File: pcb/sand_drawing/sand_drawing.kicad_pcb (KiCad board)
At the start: 2 copper layers, 75.6 x 36.2 mm, 21 parts, among them J0 12V GND, J1 Stepper1, J2 Stepper2, J3 Opto 1, J4 Opto 2, J5 ESP POWER, J6 Unused Pins, U1 WeMos_D1_mini, U2 LD1117

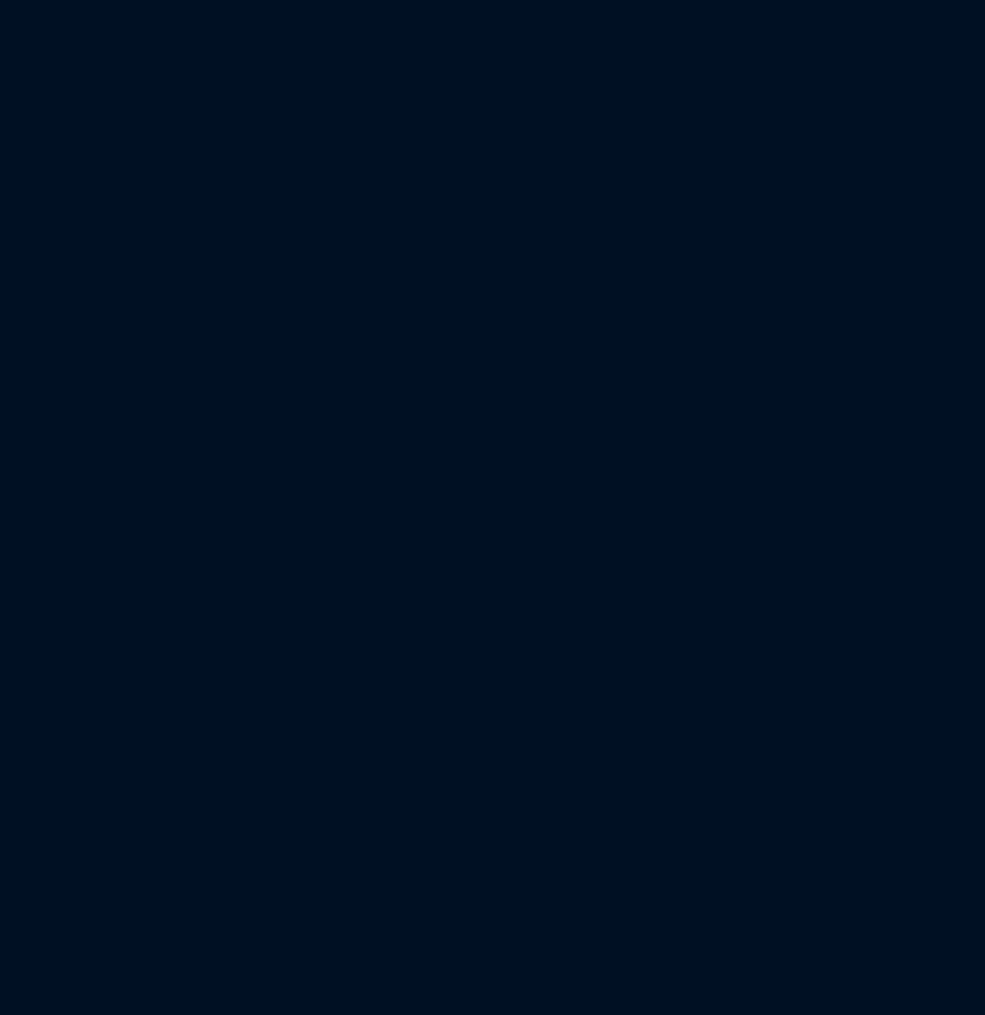
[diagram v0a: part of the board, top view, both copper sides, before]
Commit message: Start the work involved in transitioning to the ESP-WROOM-32D and TMC2100.
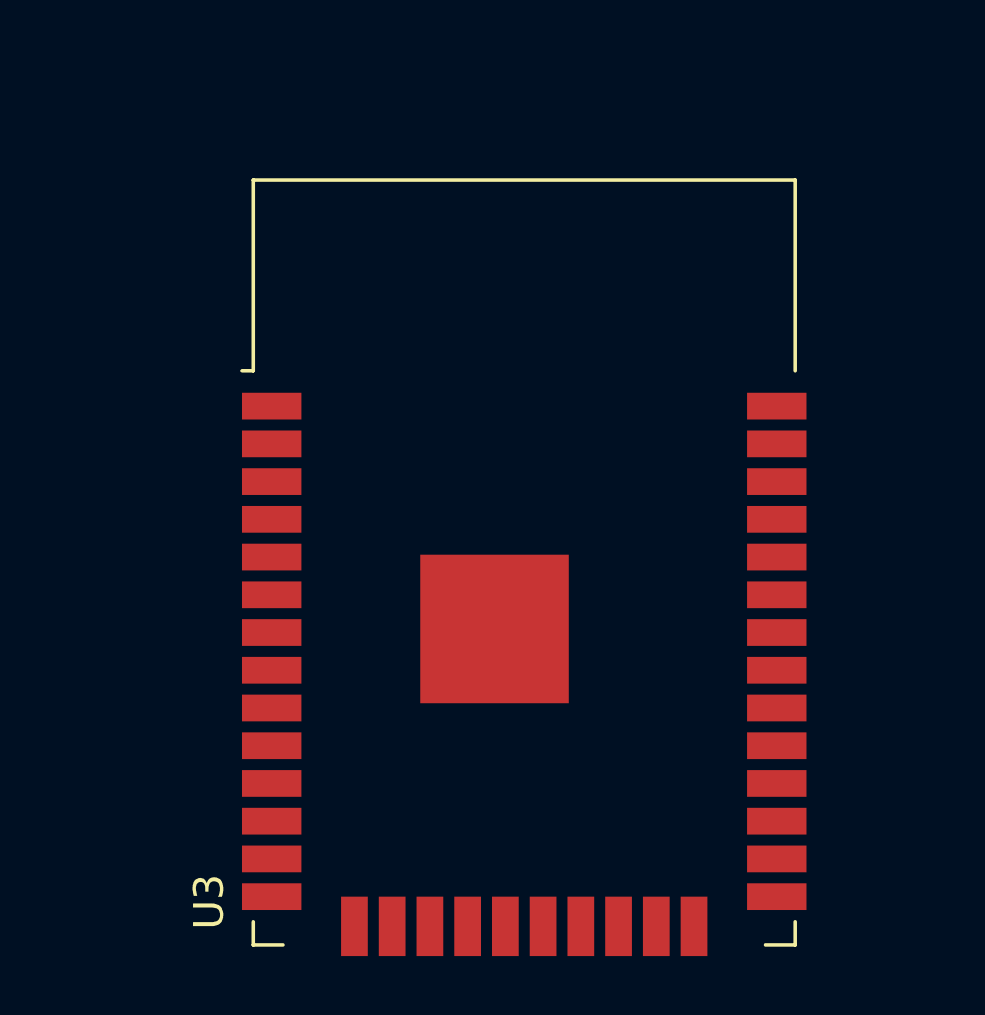
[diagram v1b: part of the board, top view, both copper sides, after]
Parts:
- added U3: ESP32-WROOM-32D, Custom:ESP32-WROOM-32, F.Cu at (154.9, 135.9)

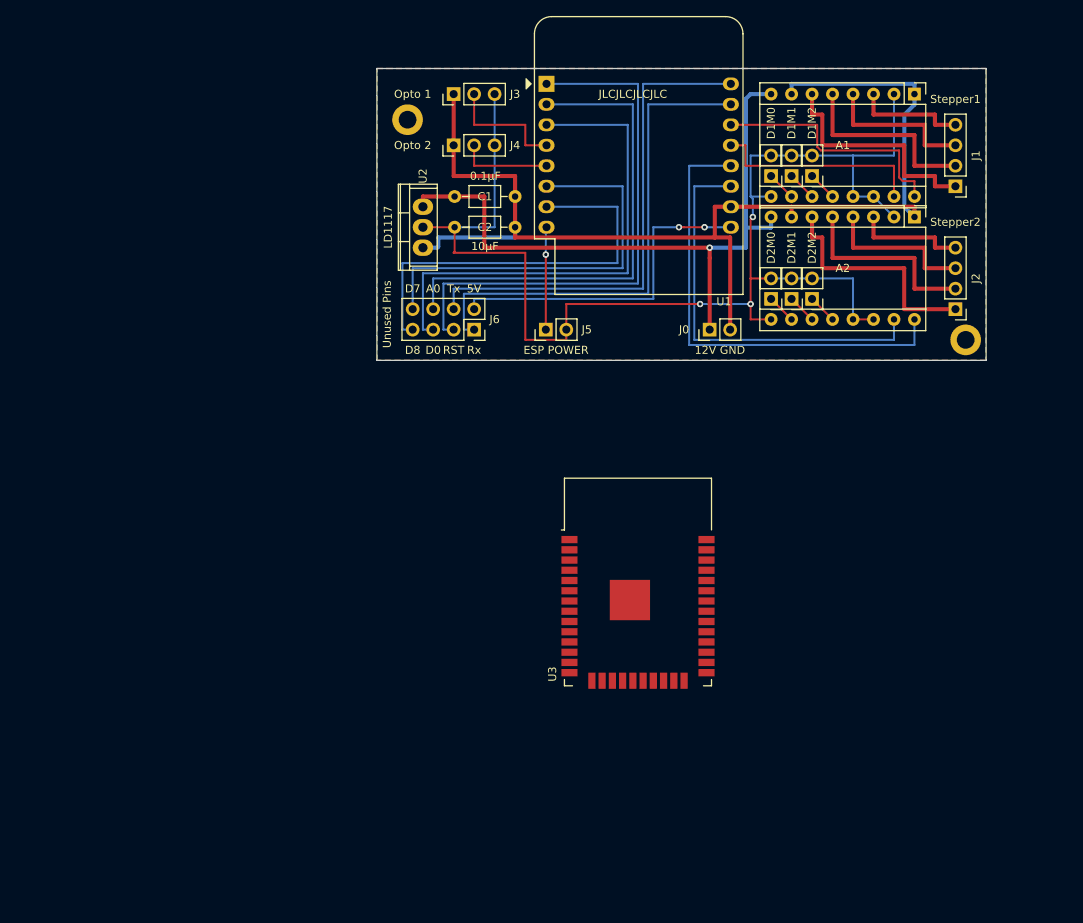
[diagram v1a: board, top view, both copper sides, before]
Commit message: Redesigned for ESP32 and TMC2100s. Lots more work to go.
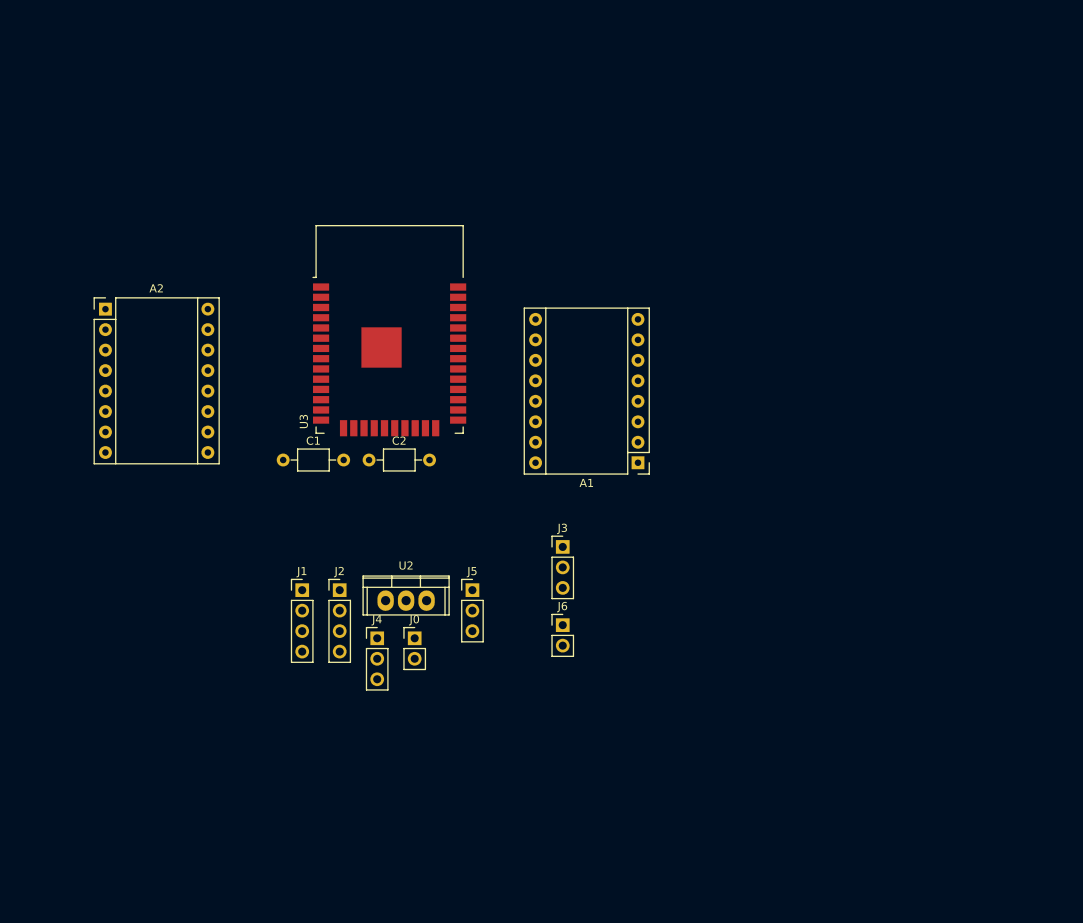
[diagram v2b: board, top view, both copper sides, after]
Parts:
- removed D1M0: Driver 1 M0, Socket_Strips:Socket_Strip_Straight_1x02_Pitch2.54mm
- removed D1M1: Driver 1 M1, Socket_Strips:Socket_Strip_Straight_1x02_Pitch2.54mm
- removed D1M2: Driver 1 M2, Socket_Strips:Socket_Strip_Straight_1x02_Pitch2.54mm
- removed D2M0: Driver 2 M0, Socket_Strips:Socket_Strip_Straight_1x02_Pitch2.54mm
- removed D2M1: Driver 2 M1, Socket_Strips:Socket_Strip_Straight_1x02_Pitch2.54mm
- removed D2M2: Driver 2 M2, Socket_Strips:Socket_Strip_Straight_1x02_Pitch2.54mm
- removed REF** (x2): MountingHole_2.2mm_M2_DIN965_Pad, MountingHole:MountingHole_2.2mm_M2_DIN965_Pad
- removed U1: WeMos_D1_mini, Custom:WEMOS_D1_mini_light
- C1: value 0.1µF -> 100µF
- J5: value ESP POWER -> UART; footprint Socket_Strips:Socket_Strip_Straight_1x02_Pitch2.54mm -> Socket_Strips:Socket_Strip_Straight_1x03_Pitch2.54mm
- J6: value Unused Pins -> ESP POWER; footprint Socket_Strips:Socket_Strip_Straight_2x04_Pitch2.54mm -> Socket_Strips:Socket_Strip_Straight_1x02_Pitch2.54mm
- moved A2 101.0 mm to (88.9, 99.1), turned to 0 degrees
- moved J1 95.2 mm to (113.3, 133.9), turned to 0 degrees
- moved J2 83.9 mm to (118.0, 133.9), turned to 0 degrees
- moved J4 61.9 mm to (122.6, 139.9), turned to 0 degrees
- moved J3 57.8 mm to (145.6, 128.6), turned to 0 degrees
- moved A1 57.1 mm to (154.9, 118.1), turned to 180 degrees
- moved J0 52.9 mm to (127.2, 139.9), turned to 0 degrees
- moved U2 46.4 mm to (126.2, 135.2), turned to 0 degrees
- moved U3 43.9 mm to (124.1, 104.6)
- moved C1 39.0 mm to (110.9, 117.8)
- moved J6 38.3 mm to (145.6, 138.2), turned to 0 degrees
- moved J5 33.6 mm to (134.4, 133.9), turned to 0 degrees
- moved C2 30.8 mm to (121.6, 117.8)
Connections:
- A1 pad 10: Net-(A1-Pad10) -> D1CFG1
- A1 pad 11: Net-(A1-Pad11) -> D1CFG2
- A1 pad 12: Net-(A1-Pad12) -> D1CFG3
- A1 pad 13: +3V3 -> Net-(A1-Pad13)
- A1 pad 14: +3V3 -> Net-(A1-Pad14)
- A1 pad 9: +3V3 -> D1Enable
- A2 pad 10: Net-(A2-Pad10) -> D2CFG1
- A2 pad 11: Net-(A2-Pad11) -> D2CFG2
- A2 pad 12: Net-(A2-Pad12) -> D2CFG3
- A2 pad 13: +3V3 -> Net-(A2-Pad13)
- A2 pad 14: +3V3 -> Net-(A2-Pad14)
- A2 pad 9: +3V3 -> D2Enable
- J3 pad 1: GND -> Net-(J3-Pad1)
- J4 pad 1: GND -> Net-(J3-Pad1)
- J5 pad 1: Net-(J5-Pad1) -> GND
- J5 pad 2: +3V3 -> RX
- J6 pad 2: Net-(J6-Pad2) -> +3V3
- U3 pad 1: Net-(U3-Pad1) -> GND
- U3 pad 10: Net-(U3-Pad10) -> D2CFG2
- U3 pad 11: Net-(U3-Pad11) -> D2CFG1
- U3 pad 12: Net-(U3-Pad12) -> D2Enable
- U3 pad 15: Net-(U3-Pad1) -> GND
- U3 pad 2: Net-(U3-Pad2) -> Net-(J6-Pad1)
- U3 pad 25: Net-(U3-Pad25) -> Reserved
- U3 pad 26: Net-(U3-Pad26) -> D1Dir
- U3 pad 27: Net-(U3-Pad27) -> D1Step
- U3 pad 28: Net-(U3-Pad28) -> D1CFG3
- U3 pad 29: Net-(U3-Pad29) -> D1CFG2
- U3 pad 3: Net-(U3-Pad3) -> Reserved
- U3 pad 30: Net-(U3-Pad30) -> D1CFG1
- U3 pad 31: Net-(U3-Pad31) -> D1Enable
- U3 pad 34: Net-(U3-Pad34) -> RX
- U3 pad 35: Net-(U3-Pad35) -> TX
- U3 pad 38: Net-(U3-Pad1) -> GND
- U3 pad 39: Net-(U3-Pad1) -> GND
- U3 pad 4: Net-(U3-Pad4) -> Opto1
- U3 pad 5: Net-(U3-Pad5) -> Opto2
- U3 pad 7: Net-(U3-Pad7) -> D2Dir
- U3 pad 8: Net-(U3-Pad8) -> D2Step
- U3 pad 9: Net-(U3-Pad9) -> D2CFG3
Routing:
- net +3V3: track 163.3 -> 0.00 mm, vias 3 -> 0
- net GND: track 142.6 -> 0.00 mm
- net +12V: track 84.1 -> 0.00 mm, vias 1 -> 0
- net Net-(J6-Pad3): track 67.2 -> 0.00 mm
- net Net-(J6-Pad1): track 62.3 -> 0.00 mm
- net Net-(J6-Pad4): track 62.3 -> 0.00 mm
- net Net-(J6-Pad5): track 62.1 -> 0.00 mm
- net Net-(J6-Pad6): track 60.9 -> 0.00 mm
- net D2Dir: track 58.5 -> 0.00 mm
- net Net-(J6-Pad7): track 52.0 -> 0.00 mm
- net D2Step: track 50.9 -> 0.00 mm
- net Net-(J6-Pad8): track 50.7 -> 0.00 mm
- net Net-(J6-Pad2): track 42.0 -> 0.00 mm, vias 2 -> 0
- net D1Dir: track 31.1 -> 0.00 mm
- net Net-(A2-Pad6): track 28.4 -> 0.00 mm
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- removed copper zone on B.Cu, net GND
- removed copper zone on F.Cu, net GND
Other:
- board outline removed
- board text removed: "5V"
- board text removed: "A0"
- board text removed: "D0"
- board text removed: "D7"
- board text removed: "D8"
- board text removed: "JLCJLCJLCJLC"
- board text removed: "RST"
- board text removed: "Rx"
- board text removed: "Tx"

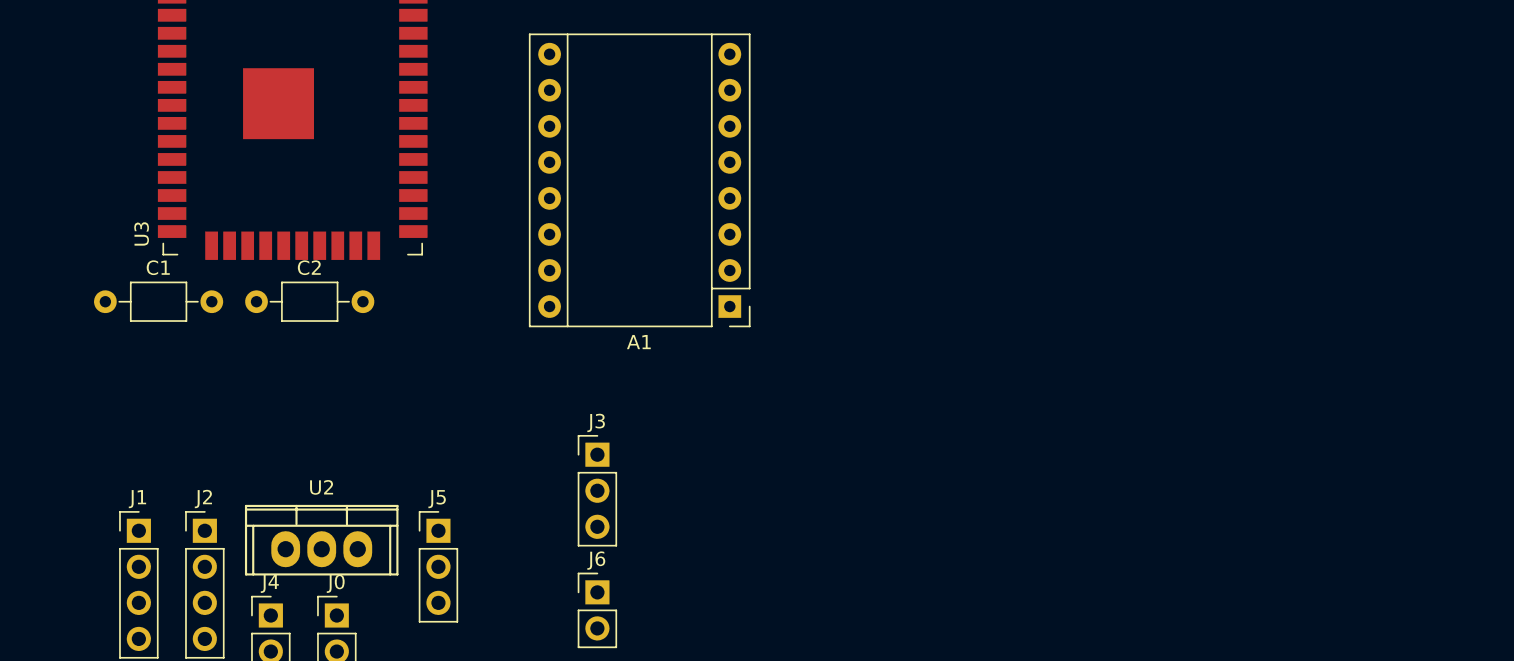
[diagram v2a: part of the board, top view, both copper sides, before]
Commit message: Assigning JLCPCB parts store codes to stuff.
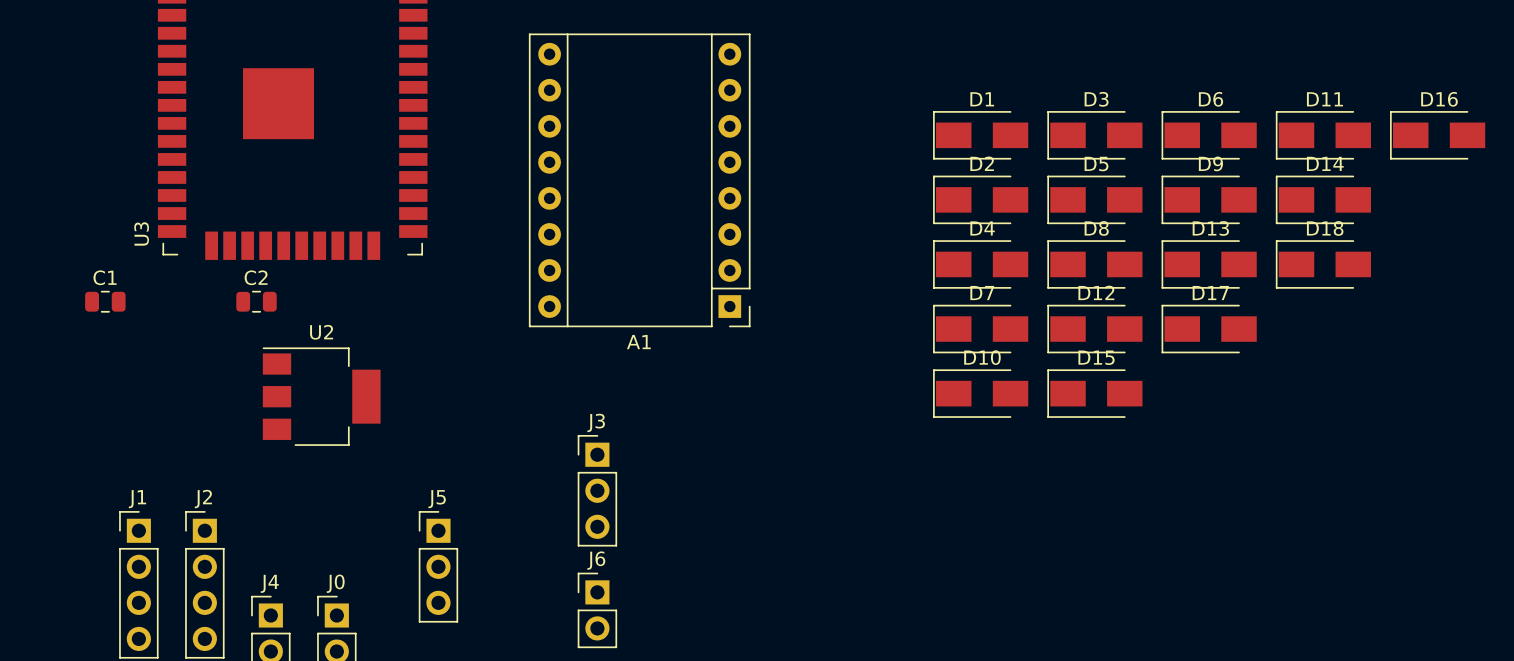
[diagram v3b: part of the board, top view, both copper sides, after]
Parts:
- added D1: SS210 Schottky Diode, Diode_SMD:D_SMA, F.Cu at (172.7, 106.0)
- added D10: SS210 Schottky Diode, Diode_SMD:D_SMA, F.Cu at (172.7, 124.2)
- added D11: SS210 Schottky Diode, Diode_SMD:D_SMA, F.Cu at (196.9, 106.0)
- added D12: SS210 Schottky Diode, Diode_SMD:D_SMA, F.Cu at (180.8, 119.7)
- added D13: SS210 Schottky Diode, Diode_SMD:D_SMA, F.Cu at (188.8, 115.1)
- added D14: SS210 Schottky Diode, Diode_SMD:D_SMA, F.Cu at (196.9, 110.6)
- added D15: SS210 Schottky Diode, Diode_SMD:D_SMA, F.Cu at (180.8, 124.2)
- added D16: SS210 Schottky Diode, Diode_SMD:D_SMA, F.Cu at (204.9, 106.0)
- added D17: SS210 Schottky Diode, Diode_SMD:D_SMA, F.Cu at (188.8, 119.7)
- added D18: SS210 Schottky Diode, Diode_SMD:D_SMA, F.Cu at (196.9, 115.1)
- added D2: SS210 Schottky Diode, Diode_SMD:D_SMA, F.Cu at (172.7, 110.6)
- added D3: SS210 Schottky Diode, Diode_SMD:D_SMA, F.Cu at (180.8, 106.0)
- added D4: SS210 Schottky Diode, Diode_SMD:D_SMA, F.Cu at (172.7, 115.1)
- added D5: SS210 Schottky Diode, Diode_SMD:D_SMA, F.Cu at (180.8, 110.6)
- added D6: SS210 Schottky Diode, Diode_SMD:D_SMA, F.Cu at (188.8, 106.0)
- added D7: SS210 Schottky Diode, Diode_SMD:D_SMA, F.Cu at (172.7, 119.7)
- added D8: SS210 Schottky Diode, Diode_SMD:D_SMA, F.Cu at (180.8, 115.1)
- added D9: SS210 Schottky Diode, Diode_SMD:D_SMA, F.Cu at (188.8, 110.6)
- C1: value 100µF -> 10µF/25V; footprint Capacitors_THT:C_Axial_L3.8mm_D2.6mm_P7.50mm_Horizontal -> Capacitor_SMD:C_0805_2012Metric
- C2: value 10µF -> 10µF/25V; footprint Capacitors_THT:C_Axial_L3.8mm_D2.6mm_P7.50mm_Horizontal -> Capacitor_SMD:C_0805_2012Metric
- U2: value LD1117 -> AMS1117-3.3; footprint Power_Integrations:TO-220 -> Package_TO_SOT_SMD:SOT-223
- moved U2 10.7 mm to (126.2, 124.5)
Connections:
- A1 pad 13: Net-(A1-Pad13) -> (no net)
- A1 pad 14: Net-(A1-Pad14) -> (no net)
- A2 pad 13: Net-(A2-Pad13) -> (no net)
- A2 pad 14: Net-(A2-Pad14) -> (no net)
- U3 pad 13: Net-(U3-Pad13) -> (no net)
- U3 pad 14: Net-(U3-Pad14) -> (no net)
- U3 pad 16: Net-(U3-Pad16) -> (no net)
- U3 pad 17: Net-(U3-Pad17) -> (no net)
- U3 pad 18: Net-(U3-Pad18) -> (no net)
- U3 pad 19: Net-(U3-Pad19) -> (no net)
- U3 pad 20: Net-(U3-Pad20) -> (no net)
- U3 pad 21: Net-(U3-Pad21) -> (no net)
- U3 pad 22: Net-(U3-Pad22) -> (no net)
- U3 pad 23: Net-(U3-Pad23) -> (no net)
- U3 pad 24: Net-(U3-Pad24) -> (no net)
- U3 pad 32: Net-(U3-Pad32) -> (no net)
- U3 pad 33: Net-(U3-Pad33) -> (no net)
- U3 pad 36: Net-(U3-Pad36) -> (no net)
- U3 pad 37: Net-(U3-Pad37) -> (no net)
- U3 pad 6: Net-(U3-Pad6) -> (no net)

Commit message: Finished hooking up the EN and IO0 buttons.
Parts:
- removed J6: ESP POWER, Socket_Strips:Socket_Strip_Straight_1x02_Pitch2.54mm
- added C3: 10µF/25V, Capacitors_SMD:C_0805, F.Cu at (128.3, 118.1)
- added R1: 10k, Capacitors_SMD:C_0603, F.Cu at (146.1, 71.1)
- added SW1: EN, Buttons_Switches_THT:SW_PUSH_6mm, F.Cu at (157.5, 74.9)
- added SW2: IO0, Buttons_Switches_THT:SW_PUSH_6mm, F.Cu at (168.0, 74.9)
- C1, C2: footprint Capacitor_SMD:C_0805_2012Metric -> Capacitors_SMD:C_0805
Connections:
- U3 pad 2: Net-(J6-Pad1) -> +3V3
- U3 pad 25: Reserved -> Net-(SW2-Pad1)
- U3 pad 3: Reserved -> Net-(C3-Pad1)
